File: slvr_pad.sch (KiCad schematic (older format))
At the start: 14 parts, among them Y1 16MHz

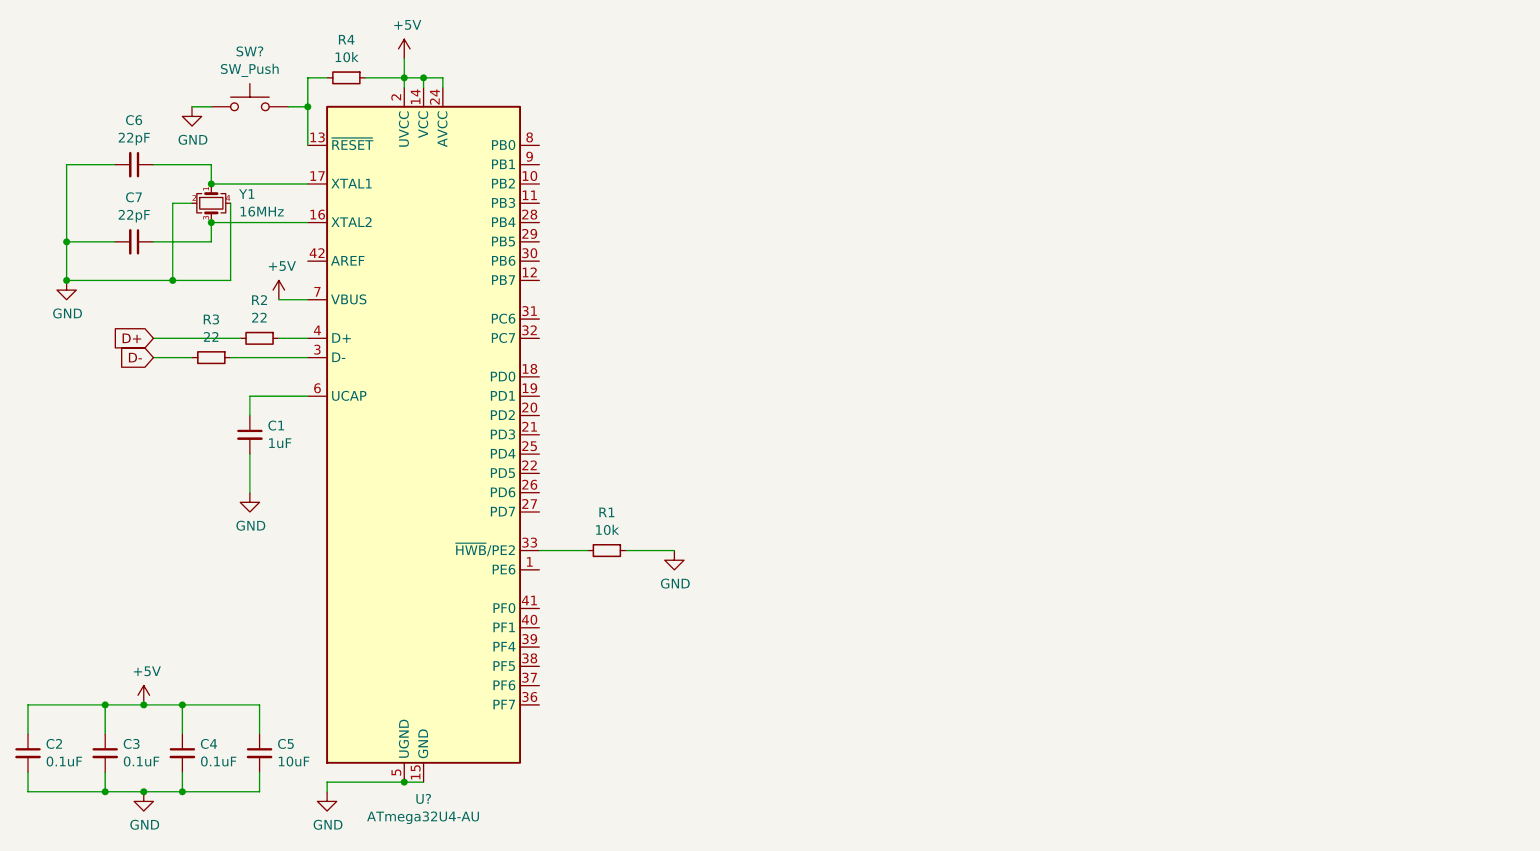
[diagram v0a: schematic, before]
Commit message: SCH: Add switch matrix and component footprints.
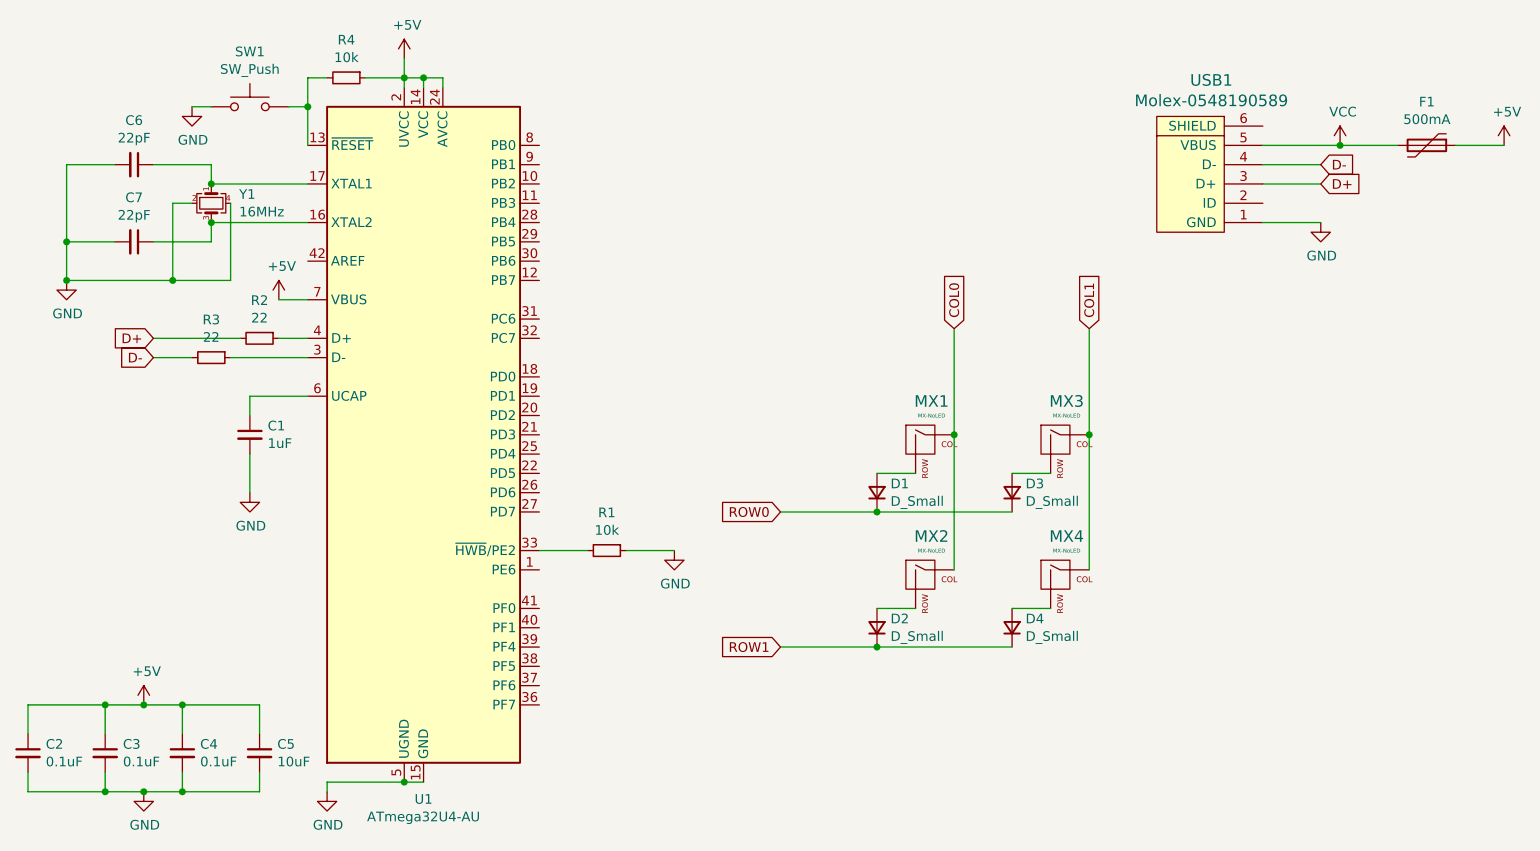
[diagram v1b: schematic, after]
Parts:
- added D1, D2, D3, D4: D_Small, Diodes_SMD:D_SOD-123, symbol Device:D_Small
- added F1: 500mA, Fuse_Holders_and_Fuses:Fuse_SMD1206_Wave, symbol Device:Polyfuse
- added MX1, MX2, MX3, MX4: MX-NoLED, MX_Alps_Hybrid:MX-1U-NoLED, symbol MX_Alps_Hybrid:MX-NoLED
- added USB1: Molex-0548190589, random-keyboard-parts:Molex-0548190589, symbol random-keyboard-parts:Molex-0548190589
- C1, C2, C3, C4, C5, C6, C7: footprint (none) -> Capacitors_SMD:C_0805
- R1, R2, R3, R4: footprint (none) -> Resistors_SMD:R_0805
- SW1: renamed from SW?; footprint (none) -> random-keyboard-parts:SKQG-1155865
- Y1: footprint (none) -> Crystals:Crystal_SMD_3225-4pin_3.2x2.5mm
- gave numbers to parts that had none: 1
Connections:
- net +5V: now also F1.1
- net D+: now also USB1.3 (D+)
- net D-: now also USB1.4 (D-)
- net GND: now also USB1.1 (GND)
- new net: D1.2 (A), MX1.2 (ROW)
- new net: D3.2 (A), MX3.2 (ROW)
- new net: D2.2 (A), MX2.2 (ROW)
- new net: D4.2 (A), MX4.2 (ROW)
- new net COL0: MX1.1 (COL), MX2.1 (COL)
- new net COL1: MX3.1 (COL), MX4.1 (COL)
- new net ROW0: D1.1 (K), D3.1 (K)
- new net ROW1: D2.1 (K), D4.1 (K)
- new net VCC: F1.2, USB1.5 (VBUS)

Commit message: PCB: Components placed
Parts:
- U1: footprint Package_QFP:TQFP-44_10x10mm_P0.8mm -> Housings_QFP:TQFP-44_10x10mm_Pitch0.8mm
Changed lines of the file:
@@
 F 0 "U1" H 2650 1361 50  0000 C CNN
 F 1 "ATmega32U4-AU" H 2650 1270 50  0000 C CNN
-F 2 "Package_QFP:TQFP-44_10x10mm_P0.8mm" H 2650 3250 50  0001 C CIN
+F 2 "Housings_QFP:TQFP-44_10x10mm_Pitch0.8mm" H 2650 3250 50  0001 C CIN
 F 3 "http://ww1.microchip.com/downloads/en/DeviceDoc/Atmel-7766-8-bit-AVR-ATmega16U4-32U4_Datasheet.pdf" H 2650 3250 50  0001 C CNN
 	1    2650 3250

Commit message: PCB: Route all traces
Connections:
- net COL0: now also MX3.1 (COL), U1.28 (PB4); no longer MX2.1 (COL)
- net COL1: now also MX2.1 (COL), U1.30 (PB6); no longer MX3.1 (COL)
- net ROW0: now also D2.1 (K), U1.27 (PD7); no longer D3.1 (K)
- net ROW1: now also D3.1 (K), U1.29 (PB5); no longer D2.1 (K)
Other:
- moved on the sheet: D2, D3, MX2, MX3
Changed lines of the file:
@@
 L MX_Alps_Hybrid:MX-NoLED MX3
 U 1 1 5F042B31
+P 5250 4000
+F 0 "MX3" H 5283 4223 60  0000 C CNN
+F 1 "MX-NoLED" H 5283 4149 20  0000 C CNN
+F 2 "MX_Alps_Hybrid:MX-1U-NoLED" H 4625 3975 60  0001 C CNN
+F 3 "" H 4625 3975 60  0001 C CNN
+	1    5250 4000
+	1    0    0    -1
+$EndComp
+$Comp
+L Device:D_Small D3
+U 1 1 5F042B3B
+P 5000 4250
+F 0 "D3" V 5046 4180 50  0000 R CNN
+F 1 "D_Small" V 4955 4180 50  0000 R CNN
+F 2 "Diodes_SMD:D_SOD-123" V 5000 4250 50  0001 C CNN
+F 3 "~" V 5000 4250 50  0001 C CNN
+	1    5000 4250
+	0    -1   -1   0
+$EndComp
+Wire Wire Line
+	5900 3450 5700 3450
+$Comp
+L MX_Alps_Hybrid:MX-NoLED MX2
+U 1 1 5F04504E
 P 5950 3300
-F 0 "MX3" H 5983 3523 60  0000 C CNN
+F 0 "MX2" H 5983 3523 60  0000 C CNN
 F 1 "MX-NoLED" H 5983 3449 20  0000 C CNN
 F 2 "MX_Alps_Hybrid:MX-1U-NoLED" H 5325 3275 60  0001 C CNN
@@
 $EndComp
 $Comp
-L Device:D_Small D3
-U 1 1 5F042B3B
+L Device:D_Small D2
+U 1 1 5F045058
 P 5700 3550
-F 0 "D3" V 5746 3480 50  0000 R CNN
+F 0 "D2" V 5746 3480 50  0000 R CNN
 F 1 "D_Small" V 5655 3480 50  0000 R CNN
 F 2 "Diodes_SMD:D_SOD-123" V 5700 3550 50  0001 C CNN
 F 3 "~" V 5700 3550 50  0001 C CNN
 	1    5700 3550
-	0    -1   -1   0
-$EndComp
-Wire Wire Line
-	5900 3450 5700 3450
-$Comp
-L MX_Alps_Hybrid:MX-NoLED MX2
-U 1 1 5F04504E
-P 5250 4000
-F 0 "MX2" H 5283 4223 60  0000 C CNN
-F 1 "MX-NoLED" H 5283 4149 20  0000 C CNN
-F 2 "MX_Alps_Hybrid:MX-1U-NoLED" H 4625 3975 60  0001 C CNN
-F 3 "" H 4625 3975 60  0001 C CNN
-	1    5250 4000
-	1    0    0    -1
-$EndComp
-$Comp
-L Device:D_Small D2
-U 1 1 5F045058
-P 5000 4250
-F 0 "D2" V 5046 4180 50  0000 R CNN
-F 1 "D_Small" V 4955 4180 50  0000 R CNN
-F 2 "Diodes_SMD:D_SOD-123" V 5000 4250 50  0001 C CNN
-F 3 "~" V 5000 4250 50  0001 C CNN
-	1    5000 4250
 	0    -1   -1   0
 $EndComp
@@
 	5900 4150 5700 4150
 Wire Wire Line
-	6100 3950 6100 3250
-Connection ~ 6100 3250
-Wire Wire Line
-	6100 3250 6100 2700
-Wire Wire Line
 	5400 3950 5400 3250
 Connection ~ 5400 3250
@@
 Wire Wire Line
 	5000 3650 4500 3650
-Wire Wire Line
-	5700 4350 5000 4350
-Wire Wire Line
-	5000 4350 4500 4350
-Connection ~ 5000 4350
 Text GLabel 5400 2700 1    50   Input ~ 0
 COL0
@@
 Text GLabel 4500 4350 0    50   Input ~ 0
 ROW1
+Wire Wire Line
+	6100 2700 6100 3250
+Connection ~ 6100 3250
+Wire Wire Line
+	6100 3250 6100 3950
+Wire Wire Line
+	4500 4350 5000 4350
+Connection ~ 5000 4350
+Wire Wire Line
+	5000 4350 5700 4350
+Text GLabel 3300 2150 2    50   Input ~ 0
+COL0
+Wire Wire Line
+	3300 3650 3250 3650
+Text GLabel 3300 3650 2    50   Input ~ 0
+ROW0
+Text GLabel 3300 2350 2    50   Input ~ 0
+COL1
+Text GLabel 3300 2250 2    50   Input ~ 0
+ROW1
+Wire Wire Line
+	3300 2150 3250 2150
+Wire Wire Line
+	3300 2250 3250 2250
+Wire Wire Line
+	3250 2350 3300 2350
 $EndSCHEMATC

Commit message: PCB: Add 3D components and fix warnings
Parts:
- C1, C2, C3, C4, C5, C6, C7: footprint Capacitors_SMD:C_0805 -> Capacitor_SMD:C_0805_2012Metric
- D1, D2, D3, D4: footprint Diodes_SMD:D_SOD-123 -> Diode_SMD:D_SOD-123
- F1: footprint Fuse_Holders_and_Fuses:Fuse_SMD1206_Wave -> Fuse:Fuse_1206_3216Metric
- R1, R2, R3, R4: footprint Resistors_SMD:R_0805 -> Resistor_SMD:R_0805_2012Metric
- U1: footprint Housings_QFP:TQFP-44_10x10mm_Pitch0.8mm -> Package_QFP:TQFP-44_10x10mm_P0.8mm
- Y1: footprint Crystals:Crystal_SMD_3225-4pin_3.2x2.5mm -> Crystal:Crystal_SMD_3225-4Pin_3.2x2.5mm
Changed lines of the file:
@@
 F 0 "U1" H 2650 1361 50  0000 C CNN
 F 1 "ATmega32U4-AU" H 2650 1270 50  0000 C CNN
-F 2 "Housings_QFP:TQFP-44_10x10mm_Pitch0.8mm" H 2650 3250 50  0001 C CIN
+F 2 "Package_QFP:TQFP-44_10x10mm_P0.8mm" H 2650 3250 50  0001 C CIN
 F 3 "http://ww1.microchip.com/downloads/en/DeviceDoc/Atmel-7766-8-bit-AVR-ATmega16U4-32U4_Datasheet.pdf" H 2650 3250 50  0001 C CNN
 	1    2650 3250
@@
 F 0 "R1" V 3404 3850 50  0000 C CNN
 F 1 "10k" V 3495 3850 50  0000 C CNN
-F 2 "Resistors_SMD:R_0805" H 3600 3850 50  0001 C CNN
+F 2 "Resistor_SMD:R_0805_2012Metric" H 3600 3850 50  0001 C CNN
 F 3 "~" H 3600 3850 50  0001 C CNN
 	1    3600 3850
@@
 F 0 "R2" V 1604 2750 50  0000 C CNN
 F 1 "22" V 1695 2750 50  0000 C CNN
-F 2 "Resistors_SMD:R_0805" H 1800 2750 50  0001 C CNN
+F 2 "Resistor_SMD:R_0805_2012Metric" H 1800 2750 50  0001 C CNN
 F 3 "~" H 1800 2750 50  0001 C CNN
 	1    1800 2750
@@
 F 0 "R3" V 1354 2850 50  0000 C CNN
 F 1 "22" V 1445 2850 50  0000 C CNN
-F 2 "Resistors_SMD:R_0805" H 1550 2850 50  0001 C CNN
+F 2 "Resistor_SMD:R_0805_2012Metric" H 1550 2850 50  0001 C CNN
 F 3 "~" H 1550 2850 50  0001 C CNN
 	1    1550 2850
@@
 F 0 "C1" H 1842 3296 50  0000 L CNN
 F 1 "1uF" H 1842 3205 50  0000 L CNN
-F 2 "Capacitors_SMD:C_0805" H 1750 3250 50  0001 C CNN
+F 2 "Capacitor_SMD:C_0805_2012Metric" H 1750 3250 50  0001 C CNN
 F 3 "~" H 1750 3250 50  0001 C CNN
 	1    1750 3250
@@
 F 0 "C2" H 692 4946 50  0000 L CNN
 F 1 "0.1uF" H 692 4855 50  0000 L CNN
-F 2 "Capacitors_SMD:C_0805" H 600 4900 50  0001 C CNN
+F 2 "Capacitor_SMD:C_0805_2012Metric" H 600 4900 50  0001 C CNN
 F 3 "~" H 600 4900 50  0001 C CNN
 	1    600  4900
@@
 F 0 "C3" H 1092 4946 50  0000 L CNN
 F 1 "0.1uF" H 1092 4855 50  0000 L CNN
-F 2 "Capacitors_SMD:C_0805" H 1000 4900 50  0001 C CNN
+F 2 "Capacitor_SMD:C_0805_2012Metric" H 1000 4900 50  0001 C CNN
 F 3 "~" H 1000 4900 50  0001 C CNN
 	1    1000 4900
@@
 F 0 "C4" H 1492 4946 50  0000 L CNN
 F 1 "0.1uF" H 1492 4855 50  0000 L CNN
-F 2 "Capacitors_SMD:C_0805" H 1400 4900 50  0001 C CNN
+F 2 "Capacitor_SMD:C_0805_2012Metric" H 1400 4900 50  0001 C CNN
 F 3 "~" H 1400 4900 50  0001 C CNN
 	1    1400 4900
@@
 F 0 "C5" H 1892 4946 50  0000 L CNN
 F 1 "10uF" H 1892 4855 50  0000 L CNN
-F 2 "Capacitors_SMD:C_0805" H 1800 4900 50  0001 C CNN
+F 2 "Capacitor_SMD:C_0805_2012Metric" H 1800 4900 50  0001 C CNN
 F 3 "~" H 1800 4900 50  0001 C CNN
 	1    1800 4900
@@
 F 0 "Y1" V 1504 2194 50  0000 L CNN
 F 1 "16MHz" V 1595 2194 50  0000 L CNN
-F 2 "Crystals:Crystal_SMD_3225-4pin_3.2x2.5mm" H 1550 2050 50  0001 C CNN
+F 2 "Crystal:Crystal_SMD_3225-4Pin_3.2x2.5mm" H 1550 2050 50  0001 C CNN
 F 3 "~" H 1550 2050 50  0001 C CNN
 	1    1550 2050
@@
 F 0 "C6" V 921 1850 50  0000 C CNN
 F 1 "22pF" V 1012 1850 50  0000 C CNN
-F 2 "Capacitors_SMD:C_0805" H 1150 1850 50  0001 C CNN
+F 2 "Capacitor_SMD:C_0805_2012Metric" H 1150 1850 50  0001 C CNN
 F 3 "~" H 1150 1850 50  0001 C CNN
 	1    1150 1850
@@
 F 0 "C7" V 921 2250 50  0000 C CNN
 F 1 "22pF" V 1012 2250 50  0000 C CNN
-F 2 "Capacitors_SMD:C_0805" H 1150 2250 50  0001 C CNN
+F 2 "Capacitor_SMD:C_0805_2012Metric" H 1150 2250 50  0001 C CNN
 F 3 "~" H 1150 2250 50  0001 C CNN
 	1    1150 2250
@@
 F 0 "R4" V 2054 1400 50  0000 C CNN
 F 1 "10k" V 2145 1400 50  0000 C CNN
-F 2 "Resistors_SMD:R_0805" H 2250 1400 50  0001 C CNN
+F 2 "Resistor_SMD:R_0805_2012Metric" H 2250 1400 50  0001 C CNN
 F 3 "~" H 2250 1400 50  0001 C CNN
 	1    2250 1400
@@
 F 0 "F1" V 7625 1750 50  0000 C CNN
 F 1 "500mA" V 7716 1750 50  0000 C CNN
-F 2 "Fuse_Holders_and_Fuses:Fuse_SMD1206_Wave" H 7900 1550 50  0001 L CNN
+F 2 "Fuse:Fuse_1206_3216Metric" H 7900 1550 50  0001 L CNN
 F 3 "~" H 7850 1750 50  0001 C CNN
 	1    7850 1750
@@
 F 0 "D1" V 5046 3480 50  0000 R CNN
 F 1 "D_Small" V 4955 3480 50  0000 R CNN
-F 2 "Diodes_SMD:D_SOD-123" V 5000 3550 50  0001 C CNN
+F 2 "Diode_SMD:D_SOD-123" V 5000 3550 50  0001 C CNN
 F 3 "~" V 5000 3550 50  0001 C CNN
 	1    5000 3550
@@
 F 0 "D3" V 5046 4180 50  0000 R CNN
 F 1 "D_Small" V 4955 4180 50  0000 R CNN
-F 2 "Diodes_SMD:D_SOD-123" V 5000 4250 50  0001 C CNN
+F 2 "Diode_SMD:D_SOD-123" V 5000 4250 50  0001 C CNN
 F 3 "~" V 5000 4250 50  0001 C CNN
 	1    5000 4250
@@
 F 0 "D2" V 5746 3480 50  0000 R CNN
 F 1 "D_Small" V 5655 3480 50  0000 R CNN
-F 2 "Diodes_SMD:D_SOD-123" V 5700 3550 50  0001 C CNN
+F 2 "Diode_SMD:D_SOD-123" V 5700 3550 50  0001 C CNN
 F 3 "~" V 5700 3550 50  0001 C CNN
 	1    5700 3550
@@
 F 0 "D4" V 5746 4180 50  0000 R CNN
 F 1 "D_Small" V 5655 4180 50  0000 R CNN
-F 2 "Diodes_SMD:D_SOD-123" V 5700 4250 50  0001 C CNN
+F 2 "Diode_SMD:D_SOD-123" V 5700 4250 50  0001 C CNN
 F 3 "~" V 5700 4250 50  0001 C CNN
 	1    5700 4250
